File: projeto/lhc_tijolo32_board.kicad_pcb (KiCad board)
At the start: 2 copper layers, 24 x 84.5 mm, 50 parts, among them J1 USB_A, J2 OLED, J3 JTAG 10pin Connector, J4 CONN_06POLAR, J5 CONN_06POLAR, Q1 MMBT3904, Q2 MMBT3904, SW1 SW_Push, SW2 SW_Push, U1 AP2112K-3.3, U2 CH340G, U3 ESP32-WROOM-32D, U4 AP2112K-3.3, Y1 12MHz 10ppm, Y2 32k 20ppm

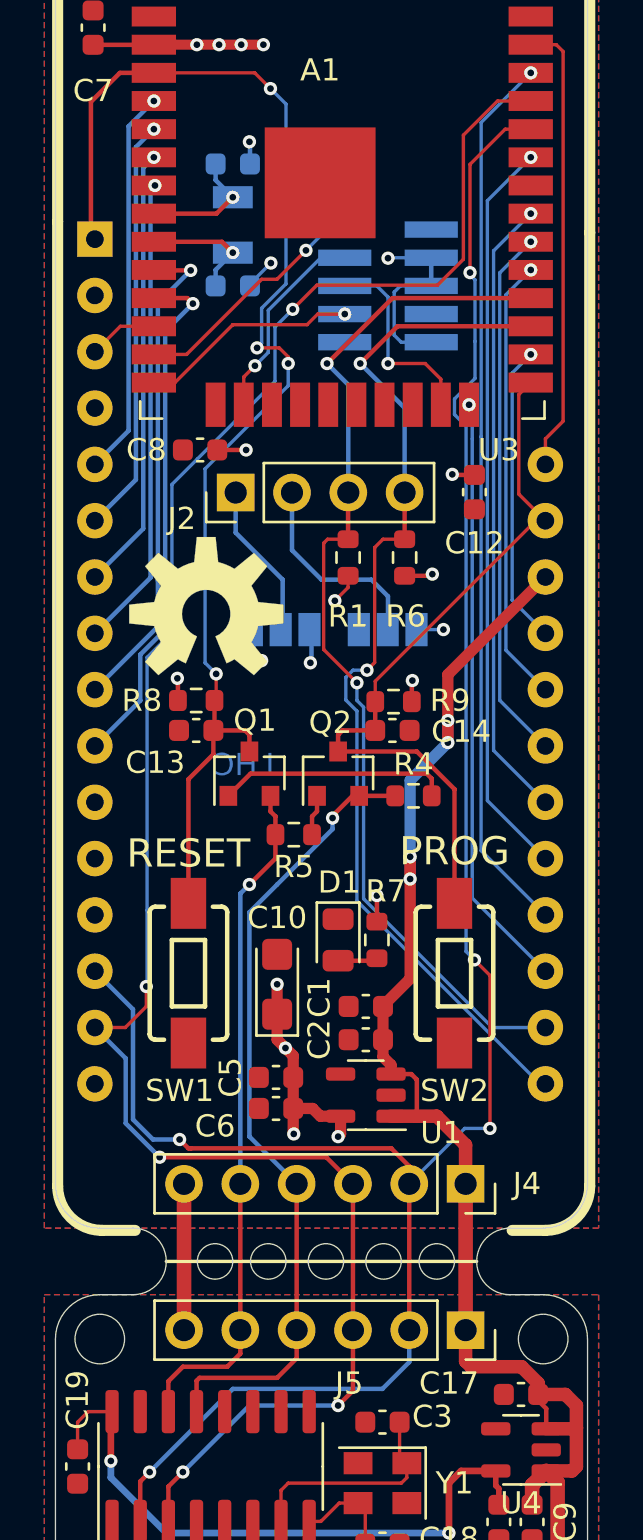
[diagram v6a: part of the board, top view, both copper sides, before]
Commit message: Updated on some labels, footprints and symbols
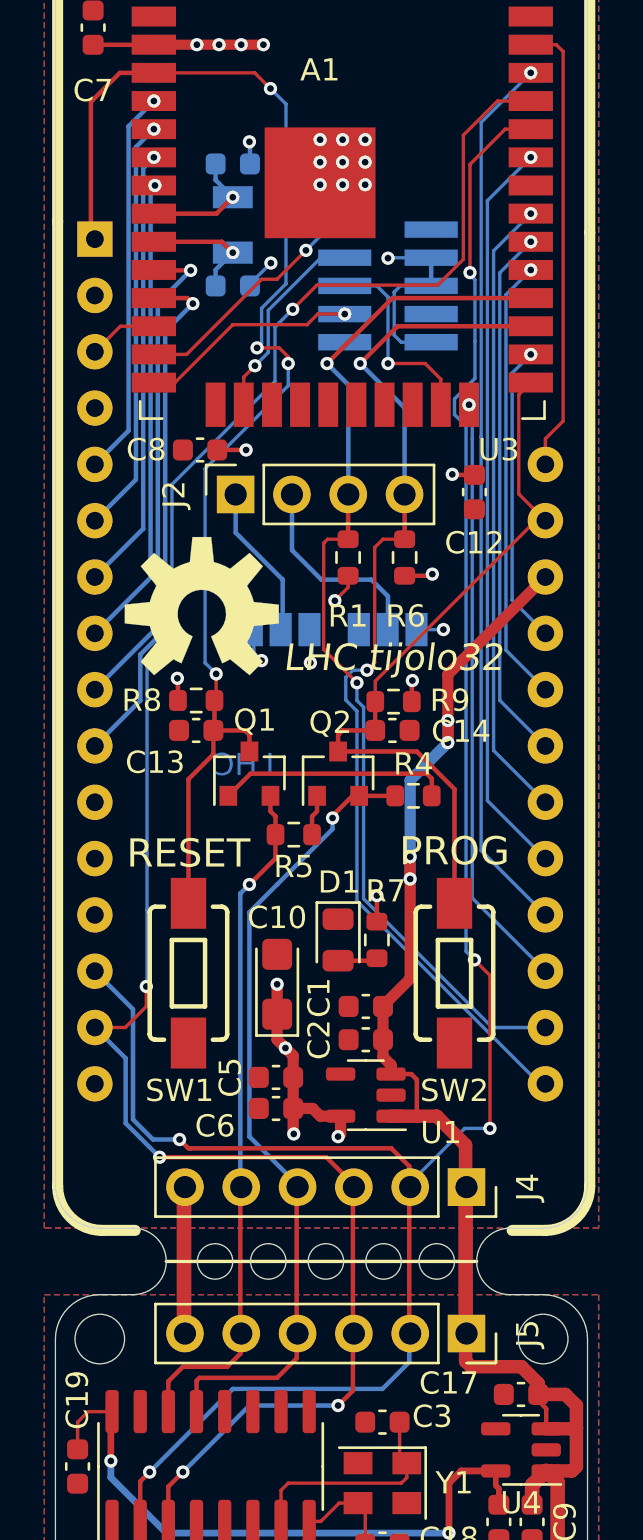
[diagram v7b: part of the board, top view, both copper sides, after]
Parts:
- J2: value OLED -> Conn_01x04; footprint Connector_PinHeader_2.54mm:PinHeader_1x04_P2.54mm_Vertical -> Connector_PinSocket_2.54mm:PinSocket_1x04_P2.54mm_Vertical
- J4, J5: value CONN_06POLAR -> Conn_01x06
- moved ? 0.20 mm to (108.2, 62.3)
- moved J5 0.16 mm to (120.1, 94.7)
- moved J4 0.15 mm to (120.1, 88.1)
- moved J2 0.09 mm to (109.7, 56.9)
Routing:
- net GND: vias 5 -> 14
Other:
- board text added: "LHC tijolo32"
